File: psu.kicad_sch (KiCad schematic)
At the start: 11 parts

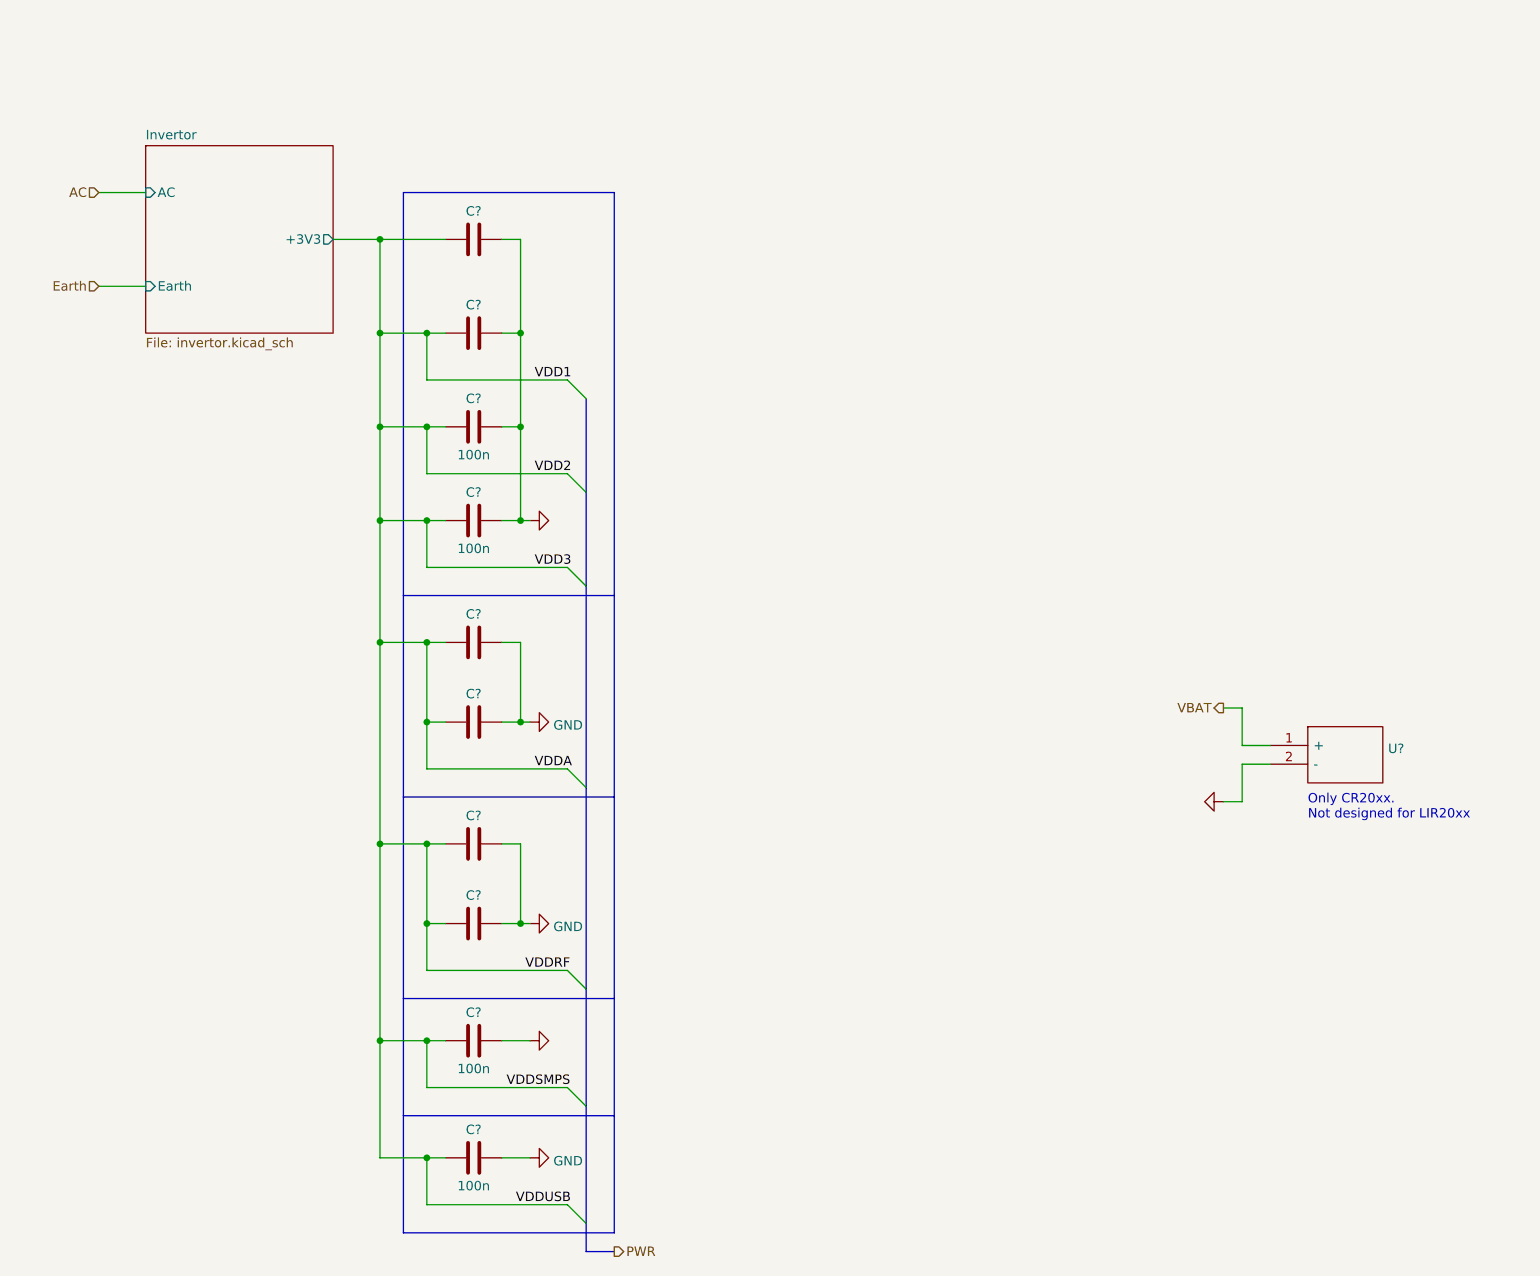
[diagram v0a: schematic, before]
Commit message: Added connectors
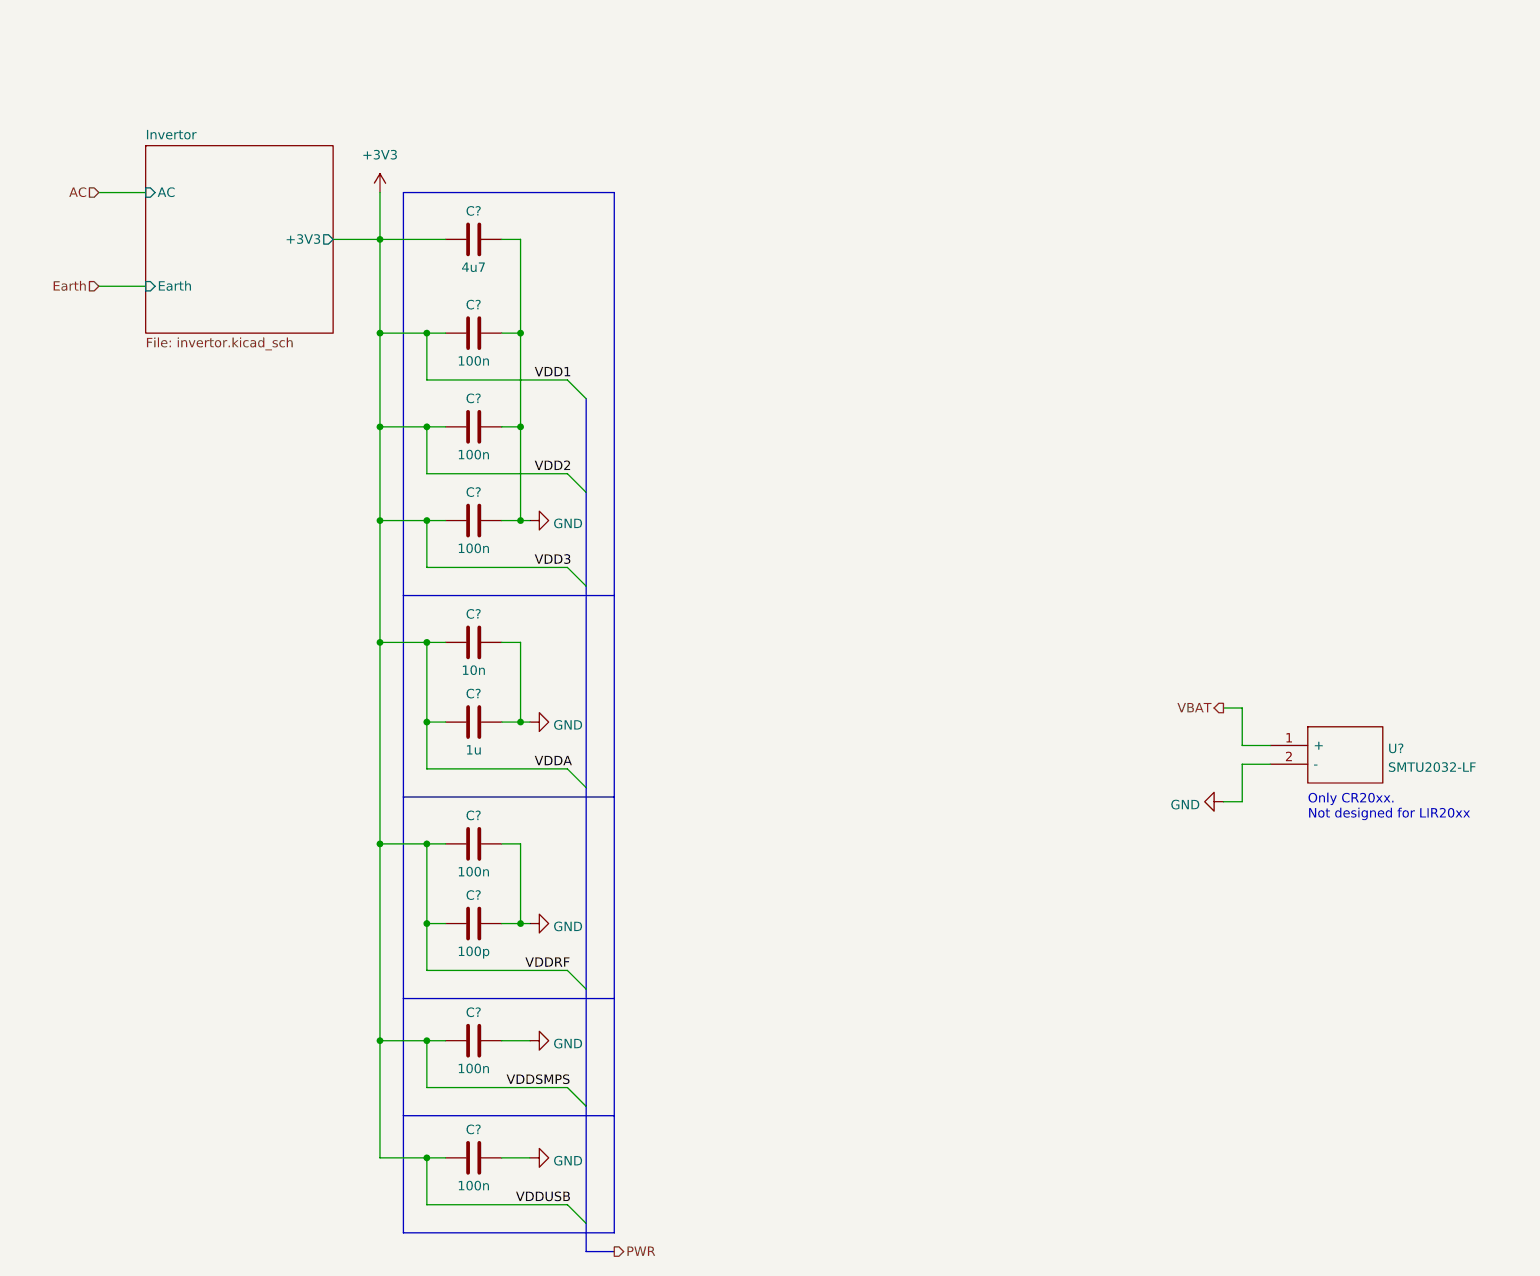
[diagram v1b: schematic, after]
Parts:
- C? (x2): value (none) -> 100n
- C?: value (none) -> 4u7
- C?: value (none) -> 10n
- C?: value (none) -> 100p
- C?: value (none) -> 1u
- U?: value (none) -> SMTU2032-LF; footprint (none) -> SMTU2032LF
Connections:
- net VDD1 renamed +3V3
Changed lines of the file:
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@@
+    (stroke (width 0) (type default) (color 0 0 0 0))
+  )
+  (wire (pts (xy 69.85 50.8) (xy 69.85 57.15))
     (stroke (width 0) (type default) (color 0 0 0 0))
   )
@@
       (effects (font (size 1.27 1.27)) hide)
     )
-    (property "Value" "" (id 1) (at 93.345 166.1688 90)
+    (property "Value" "GND" (id 1) (at 93.345 166.1688 90)
       (effects (font (size 1.27 1.27)) (justify right))
     )
@@
       (effects (font (size 1.27 1.27)) hide)
     )
-    (property "Value" "" (id 1) (at 180.9751 133.7838 90)
+    (property "Value" "GND" (id 1) (at 180.9751 133.7838 90)
       (effects (font (size 1.27 1.27)) (justify right))
     )
@@
     (in_bom yes) (on_board yes)
     (property "Reference" "C?" (id 0) (at 82.55 66.04 90))
-    (property "Value" "" (id 1) (at 82.55 73.66 90))
+    (property "Value" "100n" (id 1) (at 82.55 73.66 90))
     (property "Footprint" "" (id 2) (at 86.36 68.8848 0)
       (effects (font (size 1.27 1.27)) hide)
@@
     (in_bom yes) (on_board yes)
     (property "Reference" "C?" (id 0) (at 82.55 135.255 90))
-    (property "Value" "" (id 1) (at 82.55 142.875 90))
+    (property "Value" "100n" (id 1) (at 82.55 142.875 90))
     (property "Footprint" "" (id 2) (at 86.36 138.0998 0)
       (effects (font (size 1.27 1.27)) hide)
@@
     (pin "1")
     (pin "2")
+  )
+  (symbol (lib_id "power:+3V3") (at 69.85 50.8 0) (unit 1)
+    (in_bom yes) (on_board yes) (fields_autoplaced)
+    (property "Reference" "#PWR?" (id 0) (at 69.85 54.61 0)
+      (effects (font (size 1.27 1.27)) hide)
+    )
+    (property "Value" "+3V3" (id 1) (at 69.85 45.72 0))
+    (property "Footprint" "" (id 2) (at 69.85 50.8 0)
+      (effects (font (size 1.27 1.27)) hide)
+    )
+    (property "Datasheet" "" (id 3) (at 69.85 50.8 0)
+      (effects (font (size 1.27 1.27)) hide)
+    )
+    (pin "1")
   )
   (symbol (lib_id "OxySwitch:SMTU2032-LF") (at 190.5 125.73 0) (unit 1)
@@
       (effects (font (size 1.27 1.27)) (justify left))
     )
-    (property "Value" "" (id 1) (at 206.4512 128.7022 0)
+    (property "Value" "SMTU2032-LF" (id 1) (at 206.4512 128.7022 0)
       (effects (font (size 1.27 1.27)) (justify left))
     )
-    (property "Footprint" "" (id 2) (at 207.01 123.19 0)
+    (property "Footprint" "SMTU2032LF" (id 2) (at 207.01 123.19 0)
       (effects (font (size 1.27 1.27)) (justify left) hide)
     )
@@
     (in_bom yes) (on_board yes)
     (property "Reference" "C?" (id 0) (at 82.55 53.34 90))
-    (property "Value" "" (id 1) (at 82.55 60.96 90))
+    (property "Value" "4u7" (id 1) (at 82.55 60.96 90))
     (property "Footprint" "" (id 2) (at 86.36 56.1848 0)
       (effects (font (size 1.27 1.27)) hide)
@@
       (effects (font (size 1.27 1.27)) hide)
     )
-    (property "Value" "" (id 1) (at 93.345 95.6838 90)
+    (property "Value" "GND" (id 1) (at 93.345 95.6838 90)
       (effects (font (size 1.27 1.27)) (justify right))
     )
@@
     (in_bom yes) (on_board yes)
     (property "Reference" "C?" (id 0) (at 82.55 107.95 90))
-    (property "Value" "" (id 1) (at 82.55 115.57 90))
+    (property "Value" "10n" (id 1) (at 82.55 115.57 90))
     (property "Footprint" "" (id 2) (at 86.36 110.7948 0)
       (effects (font (size 1.27 1.27)) hide)
@@
     (in_bom yes) (on_board yes)
     (property "Reference" "C?" (id 0) (at 82.55 146.05 90))
-    (property "Value" "" (id 1) (at 82.55 153.67 90))
+    (property "Value" "100p" (id 1) (at 82.55 153.67 90))
     (property "Footprint" "" (id 2) (at 86.36 148.8948 0)
       (effects (font (size 1.27 1.27)) hide)
@@
     (in_bom yes) (on_board yes)
     (property "Reference" "C?" (id 0) (at 82.55 118.745 90))
-    (property "Value" "" (id 1) (at 82.55 126.365 90))
+    (property "Value" "1u" (id 1) (at 82.55 126.365 90))
     (property "Footprint" "" (id 2) (at 86.36 121.5898 0)
       (effects (font (size 1.27 1.27)) hide)

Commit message: ERC
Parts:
- gave numbers to parts that had none: 11
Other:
- sheet Invertor ports: added IN{PWR}; removed AC, Earth
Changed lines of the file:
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@@
-    (stroke (width 0) (type default) (color 0 0 0 0))
-  )
-  (wire (pts (xy 31.75 63.5) (xy 38.1 63.5))
     (stroke (width 0) (type default) (color 0 0 0 0))
   )
@@
     (stroke (width 0) (type default) (color 0 0 0 0))
   )
-  (wire (pts (xy 31.75 50.8) (xy 38.1 50.8))
-    (stroke (width 0) (type default) (color 0 0 0 0))
-  )
   (wire (pts (xy 69.85 95.25) (xy 76.2 95.25))
     (stroke (width 0) (type default) (color 0 0 0 0))
@@
     (stroke (width 0) (type default) (color 0 0 0 0))
   )
+  (bus (pts (xy 31.75 57.15) (xy 38.1 57.15))
+    (stroke (width 0) (type default) (color 0 0 0 0))
+  )
   (wire (pts (xy 69.85 181.61) (xy 76.2 181.61))
     (stroke (width 0) (type default) (color 0 0 0 0))
@@
     (stroke (width 0) (type default) (color 0 0 0 0))
   )
-  (wire (pts (xy 69.85 50.8) (xy 69.85 57.15))
+  (wire (pts (xy 69.85 49.53) (xy 69.85 57.15))
     (stroke (width 0) (type default) (color 0 0 0 0))
   )
@@
     (effects (font (size 1.27 1.27)) (justify left bottom))
   )
-  (hierarchical_label "Earth" (shape input) (at 31.75 63.5 180)
-    (effects (font (size 1.27 1.27)) (justify right))
-  )
-  (hierarchical_label "PWR" (shape output) (at 101.6 194.31 0)
+  (hierarchical_label "{VDD}" (shape output) (at 101.6 194.31 0)
     (effects (font (size 1.27 1.27)) (justify left))
   )
-  (hierarchical_label "AC" (shape input) (at 31.75 50.8 180)
+  (hierarchical_label "+3V3" (shape input) (at 69.85 49.53 90)
+    (effects (font (size 1.27 1.27)) (justify left))
+  )
+  (hierarchical_label "IN{PWR}" (shape input) (at 31.75 57.15 180)
     (effects (font (size 1.27 1.27)) (justify right))
   )
@@
   (symbol (lib_id "power:GND") (at 90.17 165.735 90) (unit 1)
     (in_bom yes) (on_board yes) (fields_autoplaced)
-    (property "Reference" "#PWR?" (id 0) (at 96.52 165.735 0)
+    (property "Reference" "#PWR0304" (id 0) (at 96.52 165.735 0)
       (effects (font (size 1.27 1.27)) hide)
     )
@@
   (symbol (lib_id "power:GND") (at 184.15 133.35 270) (unit 1)
     (in_bom yes) (on_board yes) (fields_autoplaced)
-    (property "Reference" "#PWR?" (id 0) (at 177.8 133.35 0)
+    (property "Reference" "#PWR0306" (id 0) (at 177.8 133.35 0)
       (effects (font (size 1.27 1.27)) hide)
     )
@@
   (symbol (lib_id "Device:C") (at 82.55 95.25 90) (unit 1)
     (in_bom yes) (on_board yes)
-    (property "Reference" "C?" (id 0) (at 82.55 91.44 90))
+    (property "Reference" "C304" (id 0) (at 82.55 91.44 90))
     (property "Value" "100n" (id 1) (at 82.55 99.06 90))
     (property "Footprint" "" (id 2) (at 86.36 94.2848 0)
@@
   (symbol (lib_id "power:GND") (at 90.17 122.555 90) (unit 1)
     (in_bom yes) (on_board yes) (fields_autoplaced)
-    (property "Reference" "#PWR?" (id 0) (at 96.52 122.555 0)
+    (property "Reference" "#PWR0302" (id 0) (at 96.52 122.555 0)
       (effects (font (size 1.27 1.27)) hide)
     )
@@
   (symbol (lib_id "power:GND") (at 90.17 181.61 90) (unit 1)
     (in_bom yes) (on_board yes) (fields_autoplaced)
-    (property "Reference" "#PWR?" (id 0) (at 96.52 181.61 0)
+    (property "Reference" "#PWR0305" (id 0) (at 96.52 181.61 0)
       (effects (font (size 1.27 1.27)) hide)
     )
@@
   (symbol (lib_id "Device:C") (at 82.55 69.85 90) (unit 1)
     (in_bom yes) (on_board yes)
-    (property "Reference" "C?" (id 0) (at 82.55 66.04 90))
+    (property "Reference" "C302" (id 0) (at 82.55 66.04 90))
     (property "Value" "100n" (id 1) (at 82.55 73.66 90))
     (property "Footprint" "" (id 2) (at 86.36 68.8848 0)
@@
   (symbol (lib_id "Device:C") (at 82.55 82.55 90) (unit 1)
     (in_bom yes) (on_board yes)
-    (property "Reference" "C?" (id 0) (at 82.55 78.74 90))
+    (property "Reference" "C303" (id 0) (at 82.55 78.74 90))
     (property "Value" "100n" (id 1) (at 82.55 86.36 90))
     (property "Footprint" "" (id 2) (at 86.36 81.5848 0)
@@
   (symbol (lib_id "Device:C") (at 82.55 165.735 90) (unit 1)
     (in_bom yes) (on_board yes)
-    (property "Reference" "C?" (id 0) (at 82.55 161.925 90))
+    (property "Reference" "C309" (id 0) (at 82.55 161.925 90))
     (property "Value" "100n" (id 1) (at 82.55 169.545 90))
     (property "Footprint" "" (id 2) (at 86.36 164.7698 0)
@@
   (symbol (lib_id "Device:C") (at 82.55 139.065 90) (unit 1)
     (in_bom yes) (on_board yes)
-    (property "Reference" "C?" (id 0) (at 82.55 135.255 90))
+    (property "Reference" "C307" (id 0) (at 82.55 135.255 90))
     (property "Value" "100n" (id 1) (at 82.55 142.875 90))
     (property "Footprint" "" (id 2) (at 86.36 138.0998 0)
@@
     (pin "2")
   )
-  (symbol (lib_id "power:+3V3") (at 69.85 50.8 0) (unit 1)
-    (in_bom yes) (on_board yes) (fields_autoplaced)
-    (property "Reference" "#PWR?" (id 0) (at 69.85 54.61 0)
-      (effects (font (size 1.27 1.27)) hide)
-    )
-    (property "Value" "+3V3" (id 1) (at 69.85 45.72 0))
-    (property "Footprint" "" (id 2) (at 69.85 50.8 0)
-      (effects (font (size 1.27 1.27)) hide)
-    )
-    (property "Datasheet" "" (id 3) (at 69.85 50.8 0)
-      (effects (font (size 1.27 1.27)) hide)
-    )
-    (pin "1")
-  )
   (symbol (lib_id "OxySwitch:SMTU2032-LF") (at 190.5 125.73 0) (unit 1)
     (in_bom yes) (on_board yes) (fields_autoplaced)
-    (property "Reference" "U?" (id 0) (at 206.4512 126.1653 0)
+    (property "Reference" "U301" (id 0) (at 206.4512 126.1653 0)
       (effects (font (size 1.27 1.27)) (justify left))
     )
@@
   (symbol (lib_id "Device:C") (at 82.55 181.61 90) (unit 1)
     (in_bom yes) (on_board yes)
-    (property "Reference" "C?" (id 0) (at 82.55 177.8 90))
+    (property "Reference" "C310" (id 0) (at 82.55 177.8 90))
     (property "Value" "100n" (id 1) (at 82.55 185.42 90))
     (property "Footprint" "" (id 2) (at 86.36 180.6448 0)
@@
   (symbol (lib_id "Device:C") (at 82.55 57.15 90) (unit 1)
     (in_bom yes) (on_board yes)
-    (property "Reference" "C?" (id 0) (at 82.55 53.34 90))
+    (property "Reference" "C301" (id 0) (at 82.55 53.34 90))
     (property "Value" "4u7" (id 1) (at 82.55 60.96 90))
     (property "Footprint" "" (id 2) (at 86.36 56.1848 0)
@@
   (symbol (lib_id "power:GND") (at 90.17 95.25 90) (unit 1)
     (in_bom yes) (on_board yes) (fields_autoplaced)
-    (property "Reference" "#PWR?" (id 0) (at 96.52 95.25 0)
+    (property "Reference" "#PWR0301" (id 0) (at 96.52 95.25 0)
       (effects (font (size 1.27 1.27)) hide)
     )
@@
   (symbol (lib_id "Device:C") (at 82.55 111.76 90) (unit 1)
     (in_bom yes) (on_board yes)
-    (property "Reference" "C?" (id 0) (at 82.55 107.95 90))
+    (property "Reference" "C305" (id 0) (at 82.55 107.95 90))
     (property "Value" "10n" (id 1) (at 82.55 115.57 90))
     (property "Footprint" "" (id 2) (at 86.36 110.7948 0)
@@
   (symbol (lib_id "Device:C") (at 82.55 149.86 90) (unit 1)
     (in_bom yes) (on_board yes)
-    (property "Reference" "C?" (id 0) (at 82.55 146.05 90))
+    (property "Reference" "C308" (id 0) (at 82.55 146.05 90))
     (property "Value" "100p" (id 1) (at 82.55 153.67 90))
     (property "Footprint" "" (id 2) (at 86.36 148.8948 0)
@@
   (symbol (lib_id "Device:C") (at 82.55 122.555 90) (unit 1)
     (in_bom yes) (on_board yes)
-    (property "Reference" "C?" (id 0) (at 82.55 118.745 90))
+    (property "Reference" "C306" (id 0) (at 82.55 118.745 90))
     (property "Value" "1u" (id 1) (at 82.55 126.365 90))
     (property "Footprint" "" (id 2) (at 86.36 121.5898 0)
@@
   (symbol (lib_id "power:GND") (at 90.17 149.86 90) (unit 1)
     (in_bom yes) (on_board yes) (fields_autoplaced)
-    (property "Reference" "#PWR?" (id 0) (at 96.52 149.86 0)
+    (property "Reference" "#PWR0303" (id 0) (at 96.52 149.86 0)
       (effects (font (size 1.27 1.27)) hide)
     )
@@
       (effects (font (size 1.27 1.27)) (justify right))
     )
-    (pin "AC" input (at 38.1 50.8 180)
+    (pin "IN{PWR}" input (at 38.1 57.15 180)
       (effects (font (size 1.27 1.27)) (justify left))
     )
-    (pin "Earth" input (at 38.1 63.5 180)
-      (effects (font (size 1.27 1.27)) (justify left))
-    )

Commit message: Schematic cleanup
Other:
- sheet Invertor ports: added 5V{PWR}; removed none
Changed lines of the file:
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@@
+    (stroke (width 0) (type default) (color 0 0 0 0))
+  )
+  (bus (pts (xy 51.435 38.1) (xy 51.435 44.45))
     (stroke (width 0) (type default) (color 0 0 0 0))
   )
@@
     (effects (font (size 1.27 1.27)) (justify left))
   )
-  (hierarchical_label "+3V3" (shape input) (at 69.85 49.53 90)
+  (hierarchical_label "+3V3" (shape output) (at 69.85 49.53 90)
     (effects (font (size 1.27 1.27)) (justify left))
   )
   (hierarchical_label "IN{PWR}" (shape input) (at 31.75 57.15 180)
     (effects (font (size 1.27 1.27)) (justify right))
+  )
+  (hierarchical_label "5V{PWR}" (shape output) (at 51.435 38.1 90)
+    (effects (font (size 1.27 1.27)) (justify left))
   )
   (hierarchical_label "VBAT" (shape output) (at 184.15 120.65 180)
@@
       (effects (font (size 1.27 1.27)) (justify left))
     )
-  )
+    (pin "5V{PWR}" input (at 51.435 44.45 90)
+      (effects (font (size 1.27 1.27)) (justify right))
+    )
+  )
